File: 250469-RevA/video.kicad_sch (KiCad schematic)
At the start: 18 parts, among them J5 DIN-8, M1 RF_Modulator, U20 8701, U21 4066, U7 8565R2, Y1 Crystal

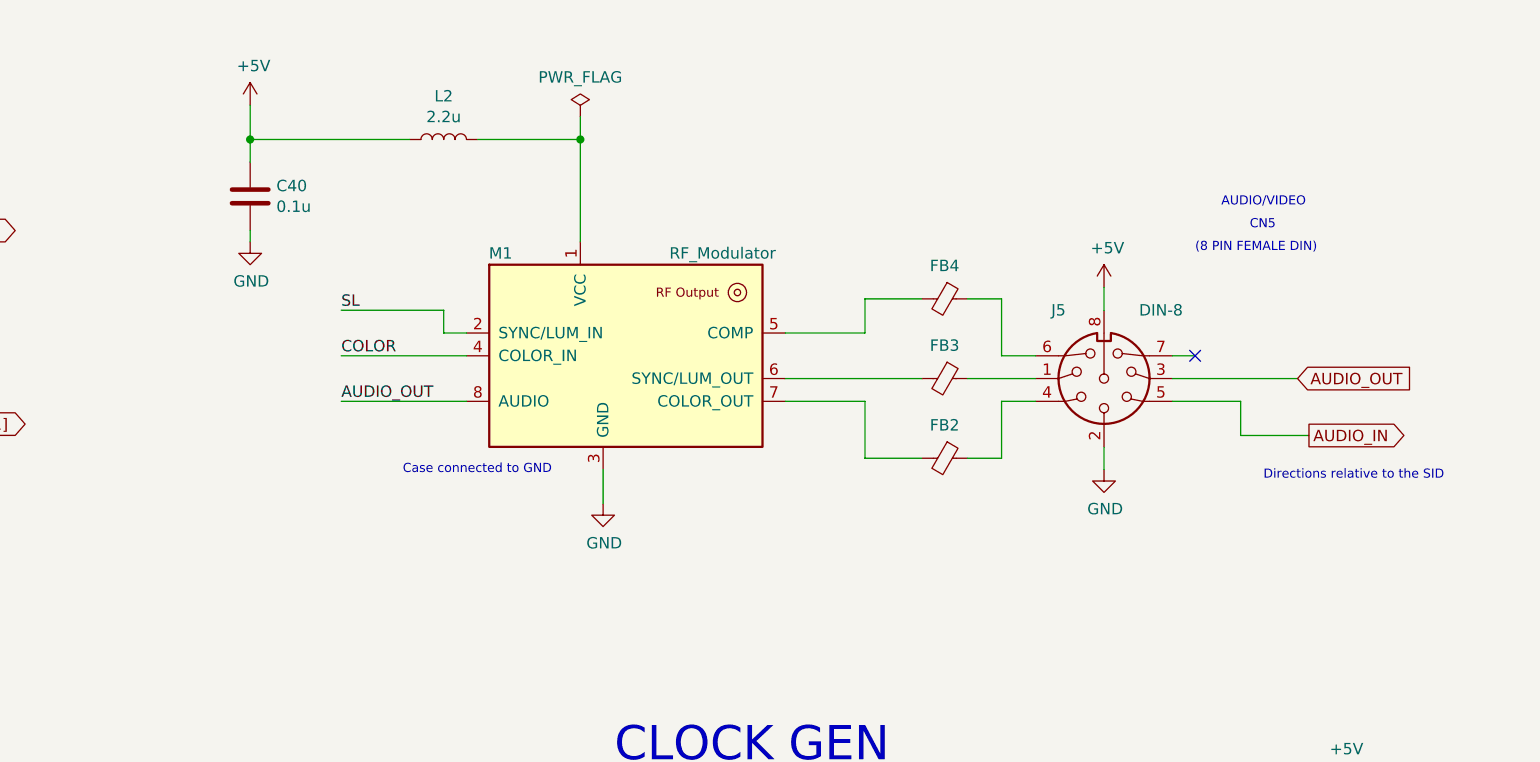
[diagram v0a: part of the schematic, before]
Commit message: Fix DIN-8 Video connector
Footprint, symbol and conections to modulator
were all wrong.
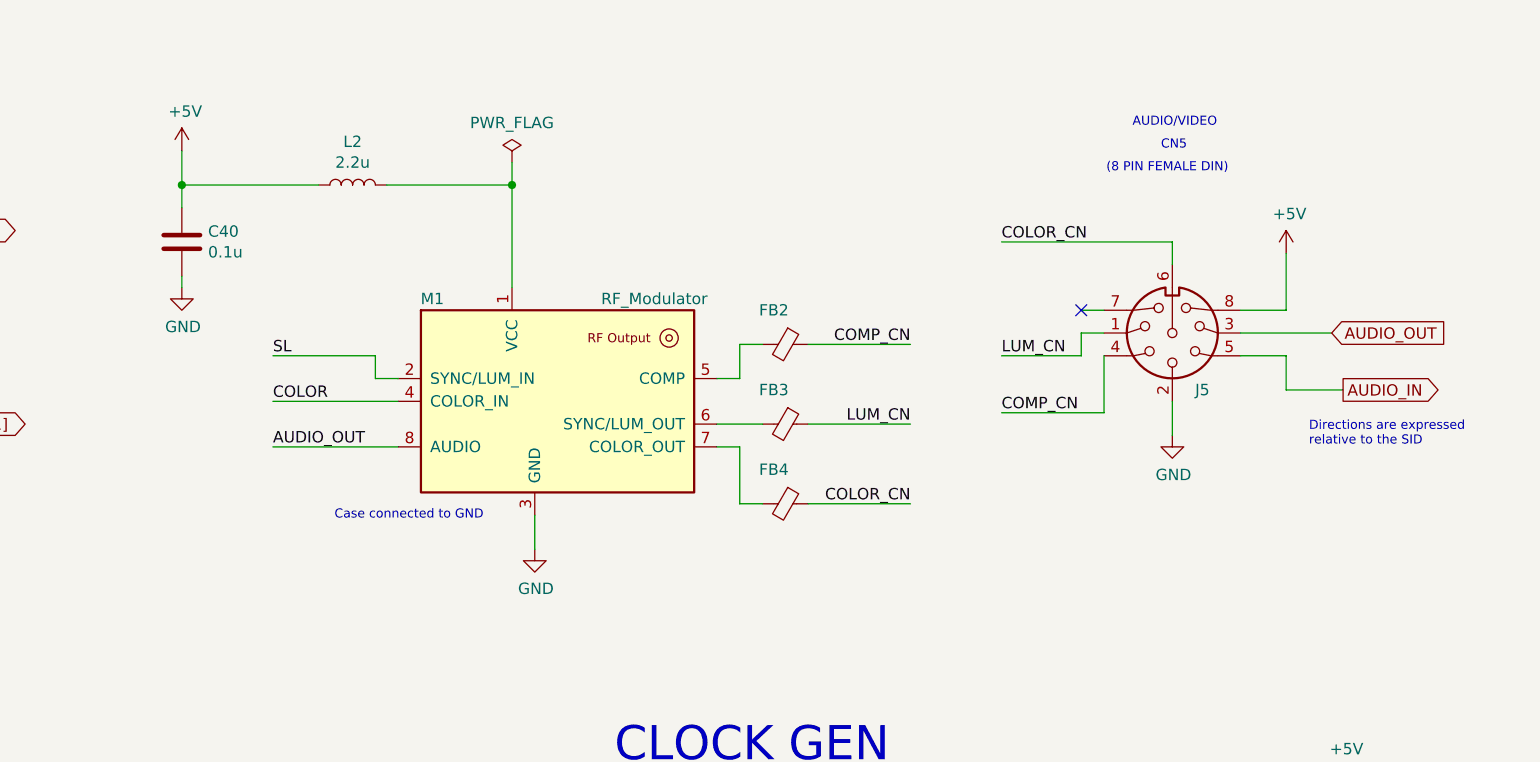
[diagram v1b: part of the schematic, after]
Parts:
- removed J5: DIN-8, krl_Connector_DIN:C64_Original_DIN-8_Circular, symbol Connector:DIN-8
- added J5: Conn_DIN-8_AudioVideo, 250469-01:Connector_DIN-8_AudioVideo, symbol 250469-01:Conn_DIN-8_AudioVideo
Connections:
- net +5V: now also J5.8
- net AUDIO_IN: now also J5.5
- net AUDIO_OUT: now also J5.3
- net GND: now also J5.2
- net COMP_CN: now reaches FB2.1
- net COMP_CN: now also J5.4
- net at FB2.2: now also M1.5 (COMP); no longer M1.7 (COLOR_OUT)
- net LUM_CN: now reaches FB3.1
- net LUM_CN: now also J5.1
- net COLOR_CN: now reaches FB4.1
- net COLOR_CN: now also J5.6
- net at FB4.2: now also M1.7 (COLOR_OUT); no longer M1.5 (COMP)
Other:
- note added: "Directions are expressed relative to the SID"
- note removed: "Directions relative to the SID"
- moved on the sheet: C40, FB2, FB3, FB4, L2, M1

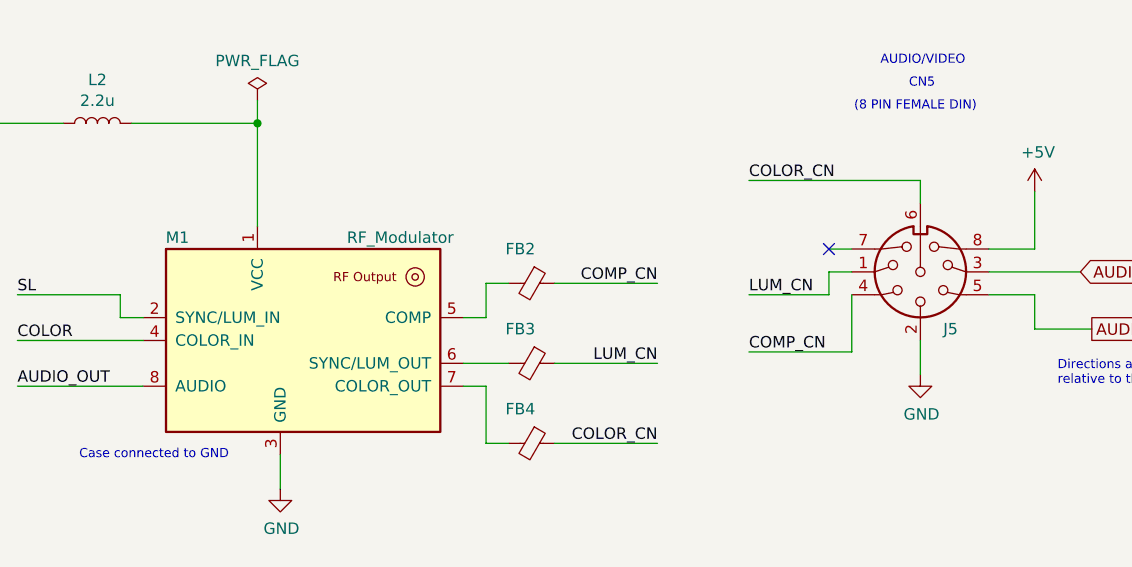
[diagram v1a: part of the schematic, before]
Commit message: Fixes after renaming the project library
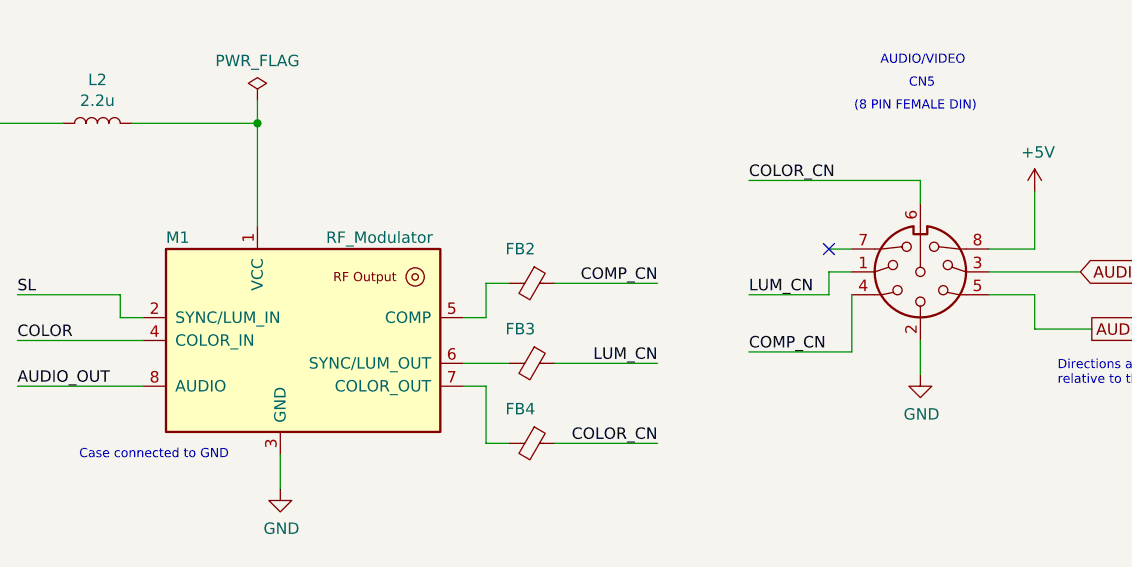
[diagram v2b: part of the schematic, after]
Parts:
- removed J5: Conn_DIN-8_AudioVideo, 250469-01:Connector_DIN-8_AudioVideo, symbol 250469-01:Conn_DIN-8_AudioVideo
- removed M1: RF_Modulator, 250469-01:RF_Modulator, symbol 250469-01:RF_Modulator
- added J5: Conn_DIN-8_AudioVideo, C64-C-250469:Connector_DIN-8_AudioVideo, symbol C64-C-250469:Conn_DIN-8_AudioVideo
- added M1: RF_Modulator, C64-C-250469:RF_Modulator, symbol C64-C-250469:RF_Modulator
- FB1: footprint 250469-01:L_Axial_Dual_L7.0mm_D3.3mm_P5.08mm_Vertical -> C64-C-250469:L_Axial_Dual_L7.0mm_D3.3mm_P5.08mm_Vertical
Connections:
- net +5V: now also J5.8
- net AUDIO_IN: now also J5.5
- net AUDIO_OUT: now also J5.3, M1.8 (AUDIO)
- net COLOR: now also M1.4 (COLOR_IN)
- net COLOR_CN: now also J5.6
- net COMP_CN: now also J5.4
- net GND: now also J5.2, M1.3 (GND)
- net LUM_CN: now also J5.1
- net SL: now also M1.2 (SYNC/LUM_IN)
- net at FB2.2: now also M1.5 (COMP)
- net at FB3.2: now also M1.6 (SYNC/LUM_OUT)
- net at FB4.2: now also M1.7 (COLOR_OUT)
- net at L2.2: now also M1.1 (VCC)
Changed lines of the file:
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@@
       (effects (font (size 1.27 1.27)))
     )
-    (property "Footprint" "250469-01:L_Axial_Dual_L7.0mm_D3.3mm_P5.08mm_Vertical" (at 227.33 142.748 90)
+    (property "Footprint" "C64-C-250469:L_Axial_Dual_L7.0mm_D3.3mm_P5.08mm_Vertical" (at 227.33 142.748 90)
       (effects (font (size 1.27 1.27)) hide)
     )
@@
         (path "/ceb6c8ef-b249-4909-95e5-e7359667aee8/00000000-0000-0000-0000-00005e427c5e"
           (reference "C40") (unit 1)
-        )
-      )
-    )
-  )
-  (symbol (lib_id "250469-01:RF_Modulator") (at 176.53 58.42 0) (unit 1)
-    (in_bom yes) (on_board yes) (dnp no)
-    (property "Reference" "M1" (at 162.56 46.99 0)
-      (effects (font (size 1.27 1.27)))
-    )
-    (property "Value" "RF_Modulator" (at 187.325 46.99 0)
-      (effects (font (size 1.27 1.27)))
-    )
-    (property "Footprint" "250469-01:RF_Modulator" (at 182.88 59.69 0)
-      (effects (font (size 1.27 1.27)) hide)
-    )
-    (property "Datasheet" "" (at 182.88 59.69 0)
-      (effects (font (size 1.27 1.27)) hide)
-    )
-    (pin "1")
-    (pin "2")
-    (pin "3")
-    (pin "4")
-    (pin "5")
-    (pin "6")
-    (pin "7")
-    (pin "8")
-    (instances
-      (project "C64C-250469-01-A"
-        (path "/ceb6c8ef-b249-4909-95e5-e7359667aee8/00000000-0000-0000-0000-00005e427c5e"
-          (reference "M1") (unit 1)
         )
       )
@@
     )
   )
-  (symbol (lib_id "250469-01:Conn_DIN-8_AudioVideo") (at 245.11 50.8 0) (mirror y) (unit 1)
-    (in_bom yes) (on_board yes) (dnp no)
-    (property "Reference" "J5" (at 247.65 57.15 0)
-      (effects (font (size 1.27 1.27)) (justify right))
-    )
-    (property "Value" "Conn_DIN-8_AudioVideo" (at 245.9989 44.45 0)
+  (symbol (lib_id "C64-C-250469:Conn_DIN-8_AudioVideo") (at 245.11 50.8 0) (mirror y) (unit 1)
+    (in_bom yes) (on_board yes) (dnp no) (fields_autoplaced)
+    (property "Reference" "J5" (at 245.9989 40.64 0)
       (effects (font (size 1.27 1.27)) (justify right) hide)
     )
-    (property "Footprint" "250469-01:Connector_DIN-8_AudioVideo" (at 245.11 50.8 0)
+    (property "Value" "Conn_DIN-8_AudioVideo" (at 245.9989 43.18 0)
+      (effects (font (size 1.27 1.27)) (justify right) hide)
+    )
+    (property "Footprint" "C64-C-250469:Connector_DIN-8_AudioVideo" (at 245.11 50.8 0)
       (effects (font (size 1.27 1.27)) hide)
     )
@@
         )
       )
+    )
+  )
+  (symbol (lib_id "C64-C-250469:RF_Modulator") (at 176.53 58.42 0) (unit 1)
+    (in_bom yes) (on_board yes) (dnp no)
+    (property "Reference" "M1" (at 161.29 46.99 0)
+      (effects (font (size 1.27 1.27)) (justify left))
+    )
+    (property "Value" "RF_Modulator" (at 179.07 46.99 0)
+      (effects (font (size 1.27 1.27)) (justify left))
+    )
+    (property "Footprint" "C64-C-250469:RF_Modulator" (at 182.88 59.69 0)
+      (effects (font (size 1.27 1.27)) hide)
+    )
+    (property "Datasheet" "" (at 182.88 59.69 0)
+      (effects (font (size 1.27 1.27)) hide)
+    )
+    (pin "1")
+    (pin "2")
+    (pin "3")
+    (pin "4")
+    (pin "5")
+    (pin "6")
+    (pin "7")
+    (pin "8")
+    (instances
+      (project "C64C-250469-01-A"
+        (path "/ceb6c8ef-b249-4909-95e5-e7359667aee8/00000000-0000-0000-0000-00005e427c5e"
+          (reference "M1") (unit 1)
+        )
+      )
